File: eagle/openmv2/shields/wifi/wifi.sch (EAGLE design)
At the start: 20 parts, among them U2 OPENMV3

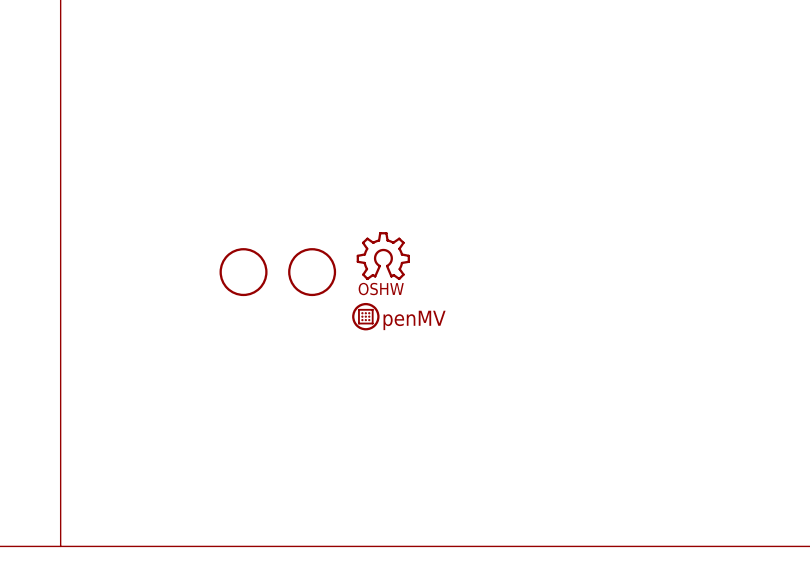
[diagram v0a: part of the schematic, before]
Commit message: Update shields silk-screen.
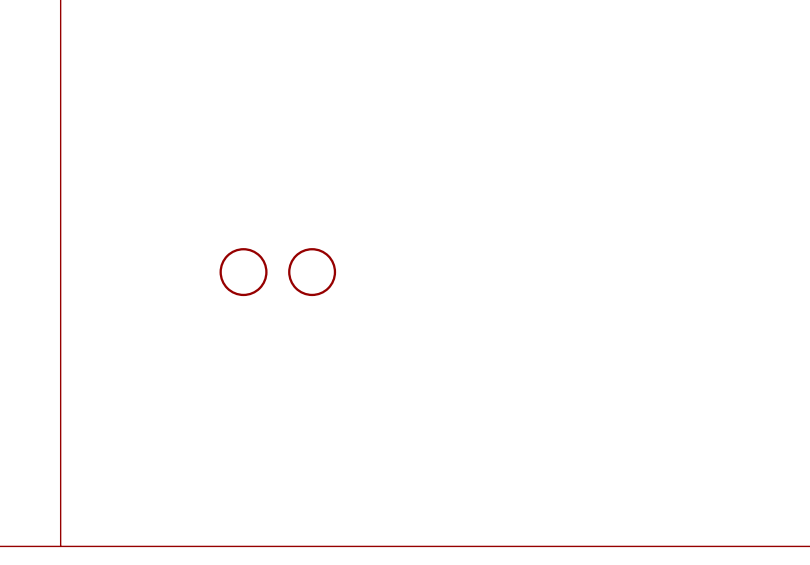
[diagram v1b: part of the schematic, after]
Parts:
- removed LOGO1: OSHW_LOGO_6MILX0150-NT, iofault:OSHW_LOGO_6MILX0150-NT
- removed U$4: OPENMV-LOGO, openmv:OPENMV-LOGO
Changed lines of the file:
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@@
 <attribute name="TP_SIGNAL_NAME" value=""/>
 </part>
-<part name="U$4" library="openmv" deviceset="OPENMV-LOGO" device=""/>
-<part name="LOGO1" library="iofault" deviceset="OSHW_LOGO_6MIL" device="X0150-NT"/>
 <part name="GND2" library="supply1" deviceset="GND" device=""/>
 <part name="R3" library="sfe" deviceset="RESISTOR" device="0603-RES" value="220R"/>
@@
 <instance part="TP2" gate="G$1" x="132.08" y="139.7"/>
 <instance part="TP3" gate="G$1" x="137.16" y="139.7"/>
-<instance part="U$4" gate="G$1" x="236.22" y="25.4"/>
-<instance part="LOGO1" gate="G$1" x="231.14" y="27.94"/>
 <instance part="GND2" gate="1" x="152.4" y="86.36"/>
 <instance part="R3" gate="G$1" x="152.4" y="116.84" smashed="yes" rot="R90">

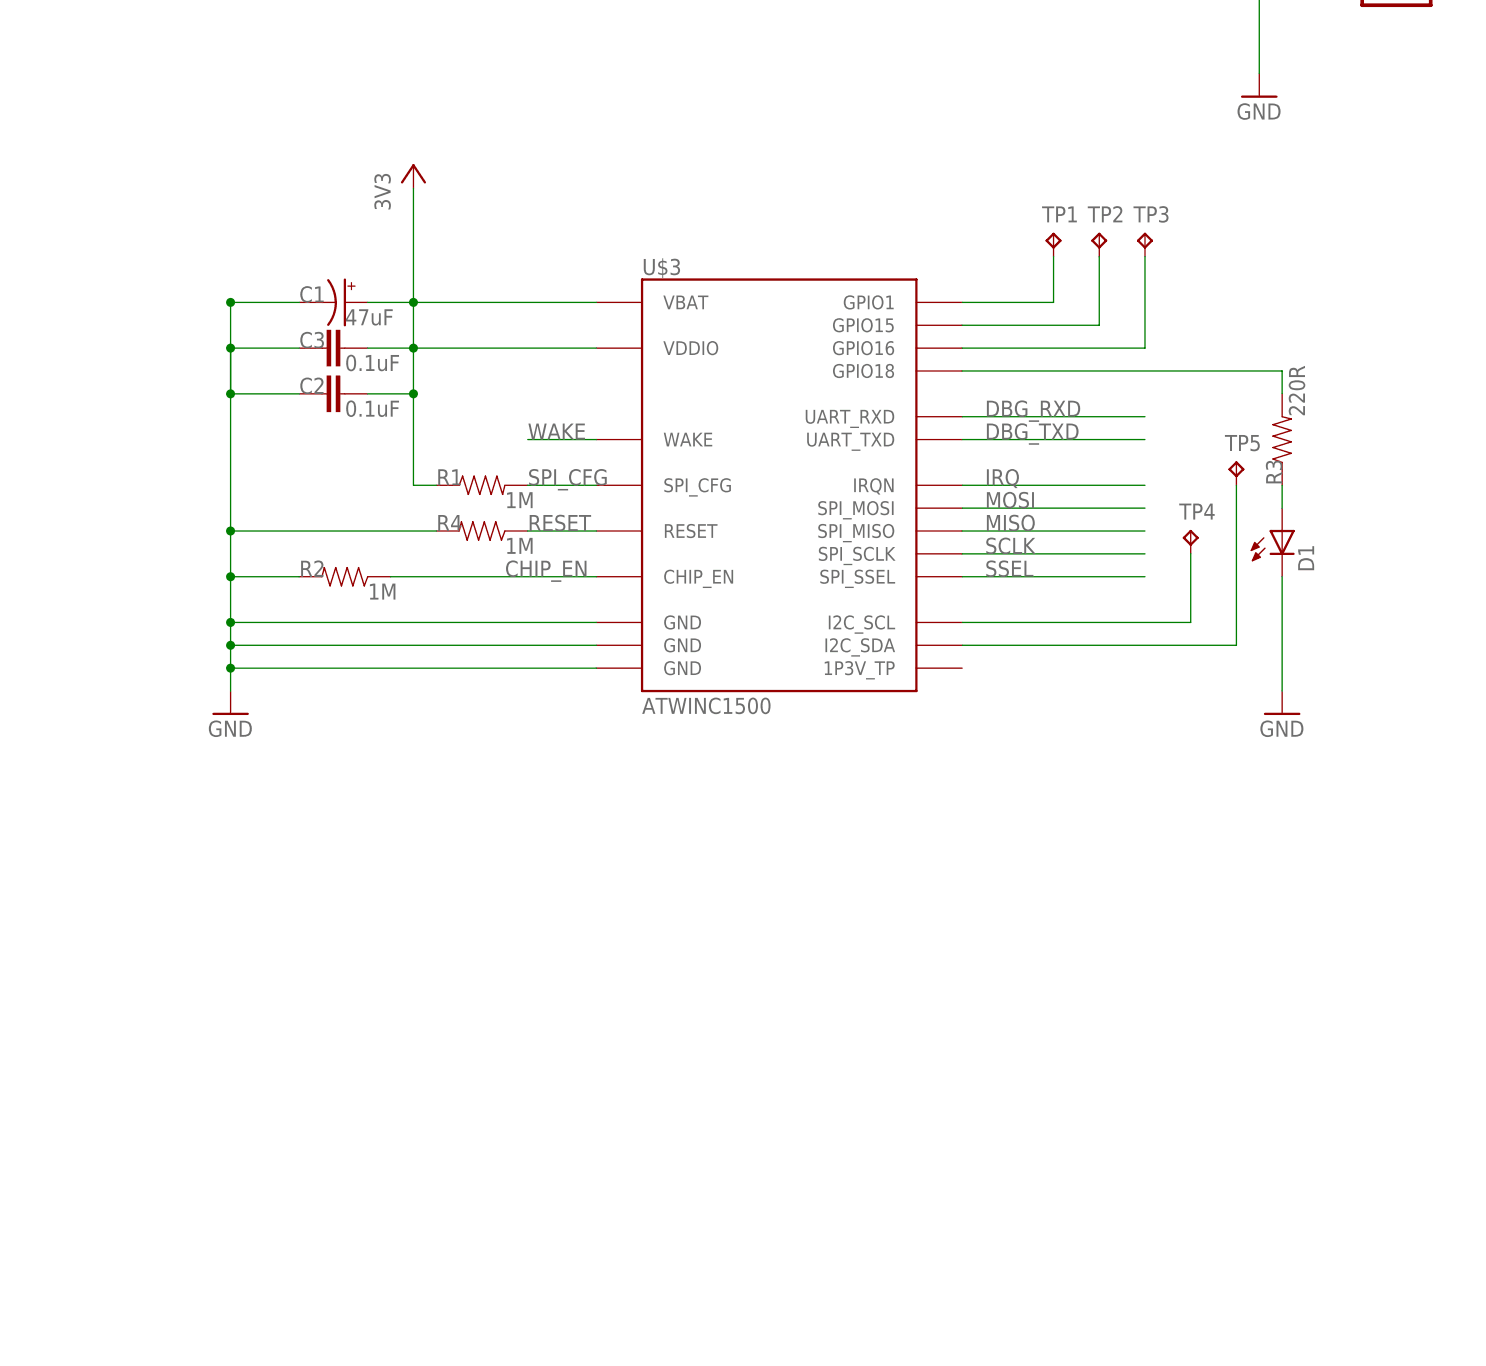
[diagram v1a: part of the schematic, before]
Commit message: Update WINC1500 to Rev-B
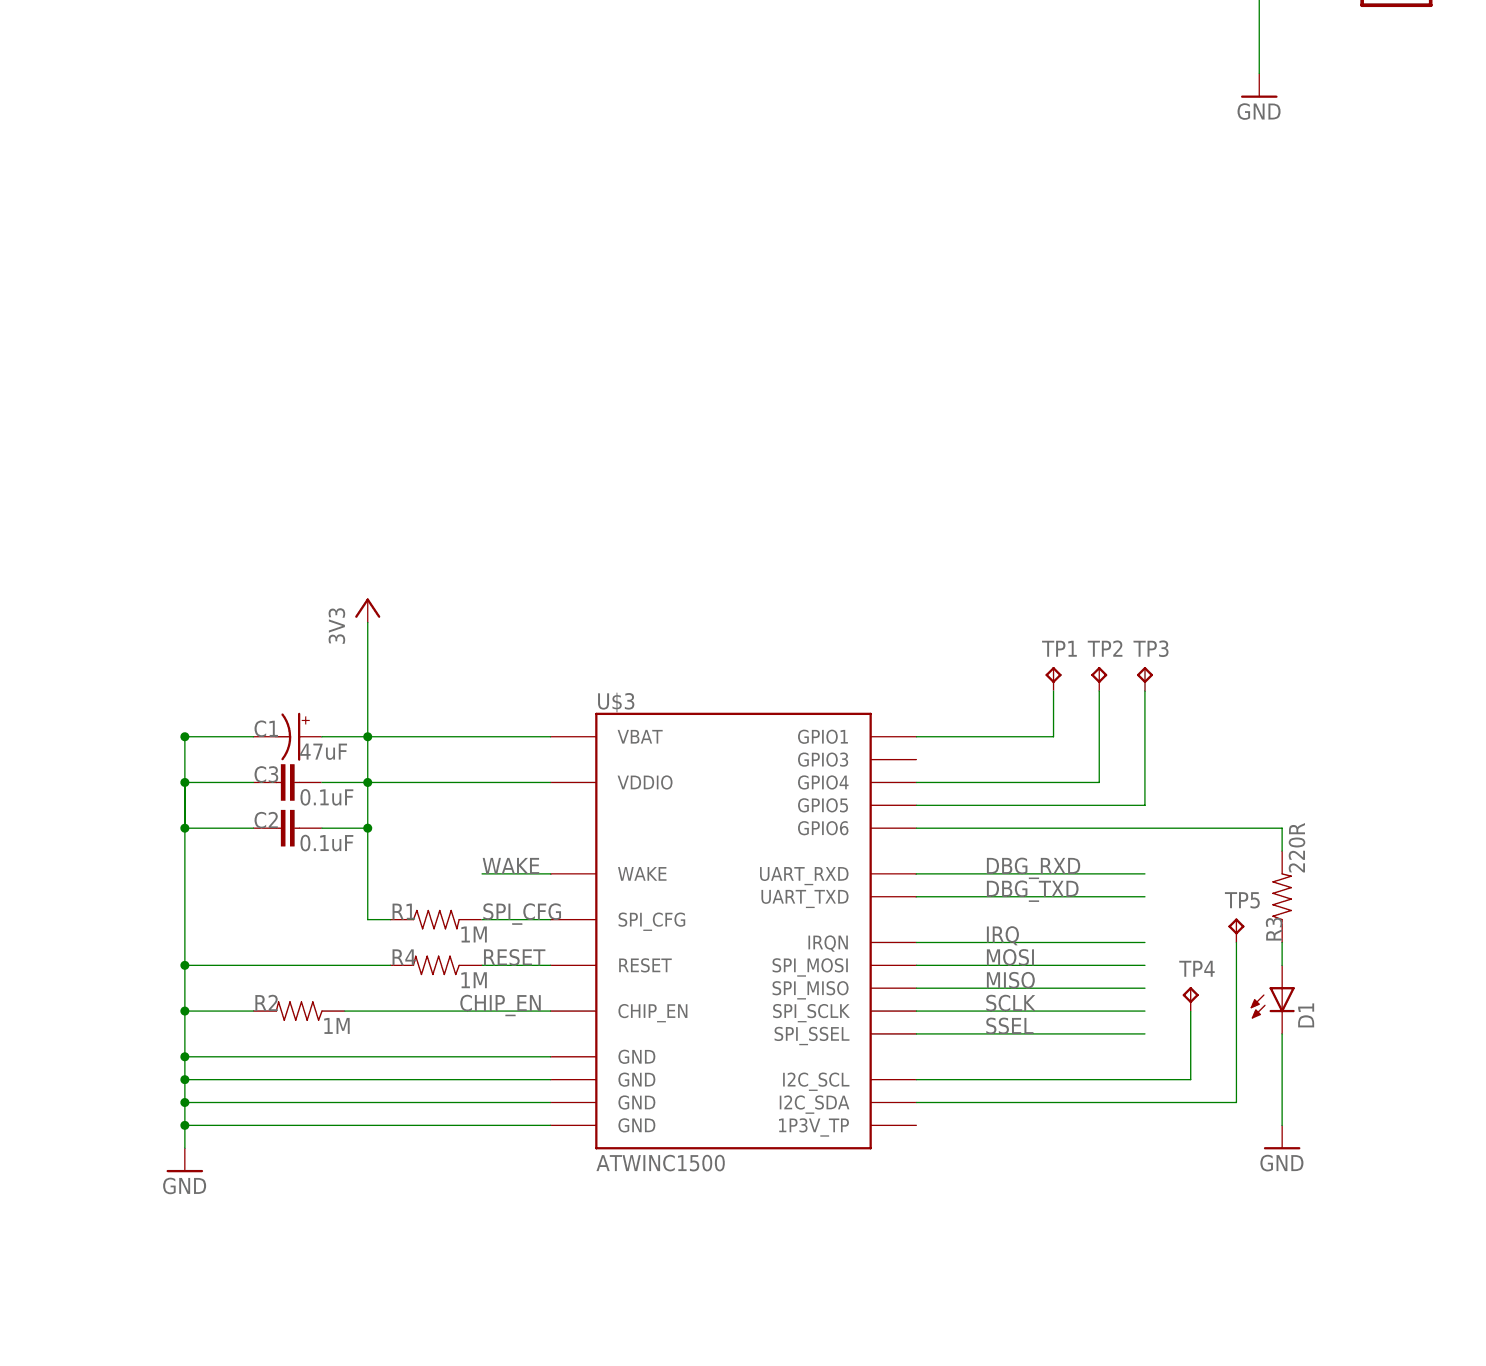
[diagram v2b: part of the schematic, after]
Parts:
- TP2, TP3: value TPTP12R -> TPTP11R; device testpad:TPTP12R -> testpad:TPTP11R
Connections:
- net GND: now also U$3.GND@4
- net N$13: now also U$3.GPIO4; no longer U$3.GPIO15
- net N$14: now also U$3.GPIO5; no longer U$3.GPIO16
- net N$15: now also U$3.GPIO6; no longer U$3.GPIO18
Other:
- moved on the sheet: C1, C2, C3, D1, R1, R2, R3, R4, TP1, TP2, TP3, TP4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
